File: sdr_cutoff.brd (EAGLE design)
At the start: 54.6 x 41.6 mm, 16 parts, among them IC1 7805T, K1 HY1Z-5V

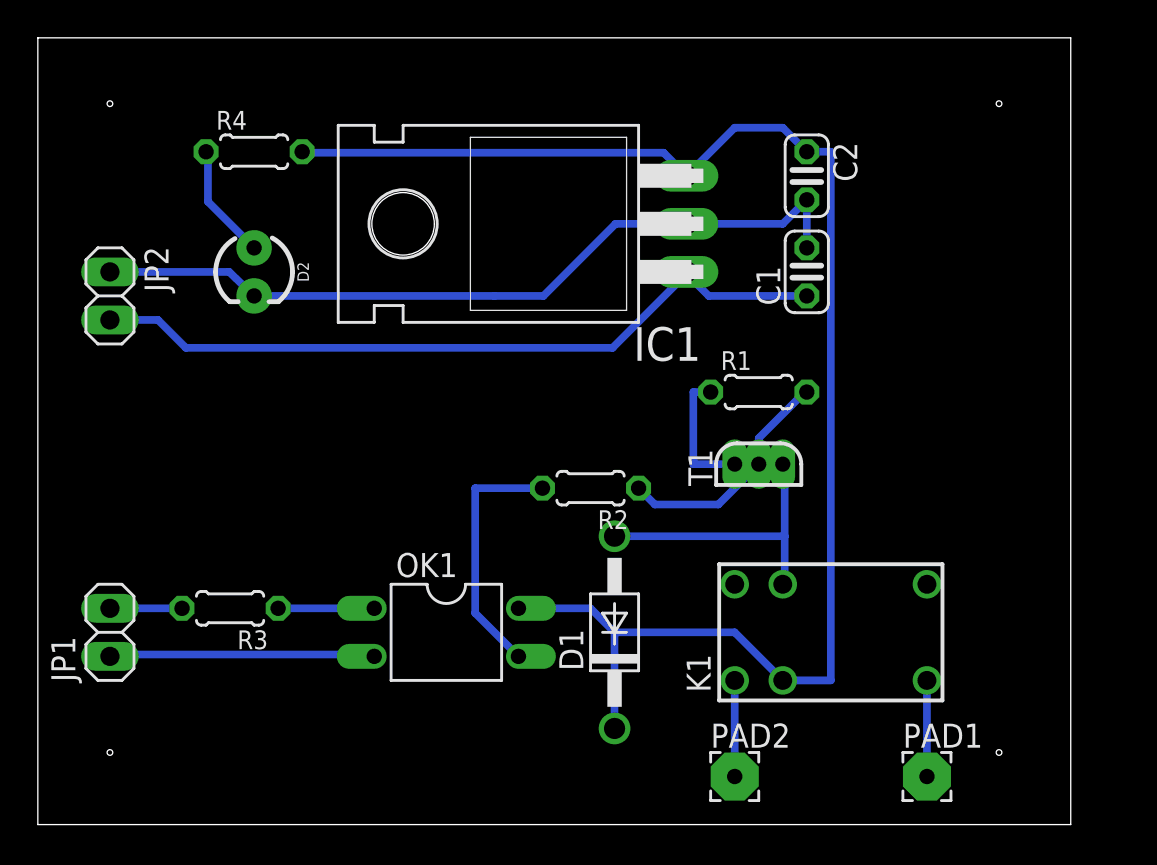
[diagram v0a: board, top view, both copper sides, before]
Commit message: Add files via upload
Corrected missing ground on DC block
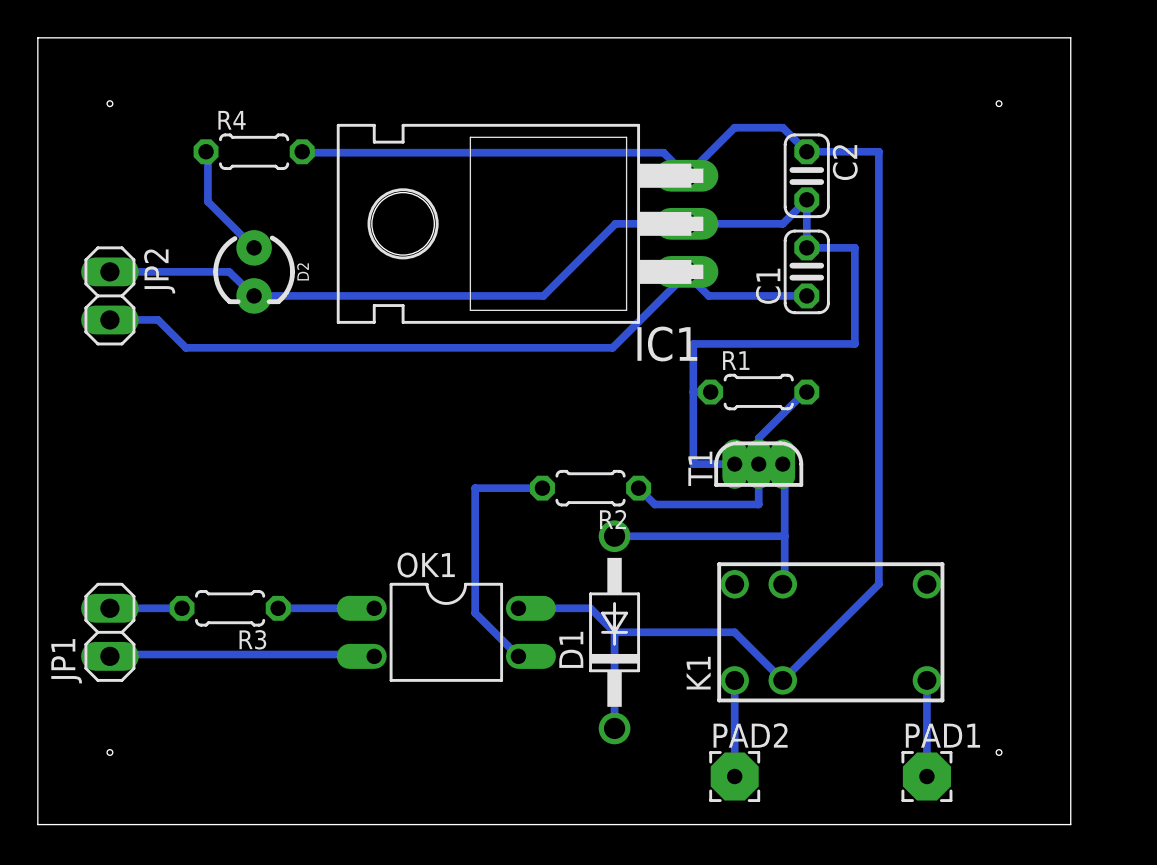
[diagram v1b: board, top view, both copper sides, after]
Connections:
- removed net N$7: C1.2, C2.2, D2.K, IC1.2, JP2.1
- net GND: now also C1.2, C2.2, D2.K, IC1.2, JP2.1
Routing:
- net GND: track 6.91 -> 67.7 mm
- net N$7: track 42.1 -> 0.00 mm
- net VCC: track 81.2 -> 83.3 mm
- net N$3: track 12.5 -> 13.8 mm
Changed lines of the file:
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@@
 <param name="rlMaxMicroViaInner" value="20mil"/>
 <param name="psTop" value="-1"/>
-<param name="psBottom" value="1"/>
+<param name="psBottom" value="2"/>
 <param name="psFirst" value="-1"/>
 <param name="psElongationLong" value="100"/>
@@
 <wire x1="40.5384" y1="22.86" x2="38.1" y2="20.4216" width="0.4064" layer="16"/>
 <wire x1="40.5384" y1="22.86" x2="40.64" y2="22.86" width="0.4064" layer="16"/>
-<wire x1="38.1" y1="19.05" x2="35.9664" y2="16.9164" width="0.4064" layer="16"/>
-<wire x1="35.9664" y1="16.9164" x2="32.6136" y2="16.9164" width="0.4064" layer="16"/>
+<wire x1="38.1" y1="19.05" x2="38.1" y2="16.9164" width="0.4064" layer="16"/>
+<wire x1="38.1" y1="16.9164" x2="32.6136" y2="16.9164" width="0.4064" layer="16"/>
 <wire x1="31.75" y1="17.78" x2="32.6136" y2="16.9164" width="0.4064" layer="16"/>
 <contactref element="T1" pad="2"/>
@@
 <contactref element="R1" pad="1"/>
 <wire x1="34.6456" y1="19.05" x2="36.83" y2="19.05" width="0.4064" layer="16"/>
+<wire x1="34.6456" y1="25.4" x2="34.6456" y2="22.86" width="0.4064" layer="16"/>
 <wire x1="34.6456" y1="22.86" x2="34.6456" y2="19.05" width="0.4064" layer="16"/>
 <wire x1="34.6456" y1="22.86" x2="35.56" y2="22.86" width="0.4064" layer="16"/>
 <contactref element="T1" pad="3"/>
+<contactref element="IC1" pad="2"/>
+<contactref element="JP2" pad="1"/>
+<contactref element="D2" pad="K"/>
+<contactref element="C2" pad="2"/>
+<contactref element="C1" pad="2"/>
+<wire x1="10.111153125" y1="29.21" x2="3.81" y2="29.21" width="0.4064" layer="16"/>
+<wire x1="10.111153125" y1="29.21" x2="11.43" y2="27.94" width="0.4064" layer="16"/>
+<wire x1="34.29" y1="31.8516" x2="34.29" y2="31.75" width="0.4064" layer="16"/>
+<wire x1="26.7208" y1="27.94" x2="11.43" y2="27.94" width="0.4064" layer="16"/>
+<wire x1="34.29" y1="31.75" x2="30.5308" y2="31.75" width="0.4064" layer="16"/>
+<wire x1="30.5308" y1="31.75" x2="26.7208" y2="27.94" width="0.4064" layer="16"/>
+<wire x1="40.64" y1="33.02" x2="40.64" y2="30.48" width="0.4064" layer="16"/>
+<wire x1="40.64" y1="33.02" x2="39.37" y2="31.75" width="0.4064" layer="16"/>
+<wire x1="39.37" y1="31.75" x2="34.29" y2="31.75" width="0.4064" layer="16"/>
+<wire x1="34.6456" y1="25.4" x2="43.18" y2="25.4" width="0.4064" layer="16"/>
+<wire x1="43.18" y1="25.4" x2="43.18" y2="30.48" width="0.4064" layer="16"/>
+<wire x1="43.18" y1="30.48" x2="40.64" y2="30.48" width="0.4064" layer="16"/>
 </signal>
 <signal name="VCC">
@@
 <wire x1="34.29" y1="34.29" x2="33.0708" y2="35.5092" width="0.4064" layer="16"/>
 <wire x1="14.0208" y1="35.5092" x2="13.97" y2="35.56" width="0.4064" layer="16"/>
-<wire x1="39.37" y1="7.62" x2="41.91" y2="7.62" width="0.4064" layer="16"/>
-<wire x1="41.91" y1="35.56" x2="41.91" y2="7.62" width="0.4064" layer="16"/>
+<wire x1="39.37" y1="7.62" x2="44.45" y2="12.7" width="0.4064" layer="16"/>
+<wire x1="44.45" y1="35.56" x2="44.45" y2="12.7" width="0.4064" layer="16"/>
 <wire x1="36.83" y1="36.83" x2="39.37" y2="36.83" width="0.4064" layer="16"/>
 <wire x1="39.37" y1="36.83" x2="40.64" y2="35.56" width="0.4064" layer="16"/>
 <wire x1="34.29" y1="34.29" x2="36.83" y2="36.83" width="0.4064" layer="16"/>
-<wire x1="40.64" y1="35.56" x2="41.91" y2="35.56" width="0.4064" layer="16"/>
+<wire x1="40.64" y1="35.56" x2="44.45" y2="35.56" width="0.4064" layer="16"/>
 </signal>
 <signal name="N$2">
@@
 <wire x1="3.81" y1="11.43" x2="7.62" y2="11.43" width="0.4064" layer="16"/>
 </signal>
-<signal name="N$7">
-<contactref element="IC1" pad="2"/>
-<contactref element="JP2" pad="1"/>
-<contactref element="D2" pad="K"/>
-<contactref element="C2" pad="2"/>
-<contactref element="C1" pad="2"/>
-<wire x1="10.111153125" y1="29.21" x2="3.81" y2="29.21" width="0.4064" layer="16"/>
-<wire x1="10.111153125" y1="29.21" x2="11.43" y2="27.94" width="0.4064" layer="16"/>
-<wire x1="34.29" y1="31.8516" x2="34.29" y2="31.75" width="0.4064" layer="16"/>
-<wire x1="26.7208" y1="27.94" x2="24.13" y2="27.94" width="0.4064" layer="16"/>
-<wire x1="24.13" y1="27.94" x2="11.43" y2="27.94" width="0.4064" layer="16"/>
-<wire x1="34.29" y1="31.75" x2="30.5308" y2="31.75" width="0.4064" layer="16"/>
-<wire x1="30.5308" y1="31.75" x2="26.7208" y2="27.94" width="0.4064" layer="16"/>
-<wire x1="40.64" y1="33.02" x2="40.64" y2="30.48" width="0.4064" layer="16"/>
-<wire x1="40.64" y1="33.02" x2="39.37" y2="31.75" width="0.4064" layer="16"/>
-<wire x1="39.37" y1="31.75" x2="34.29" y2="31.75" width="0.4064" layer="16"/>
-</signal>
 <signal name="N$8">

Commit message: Add files via upload
Corrected minor errors and finalised PCB layout
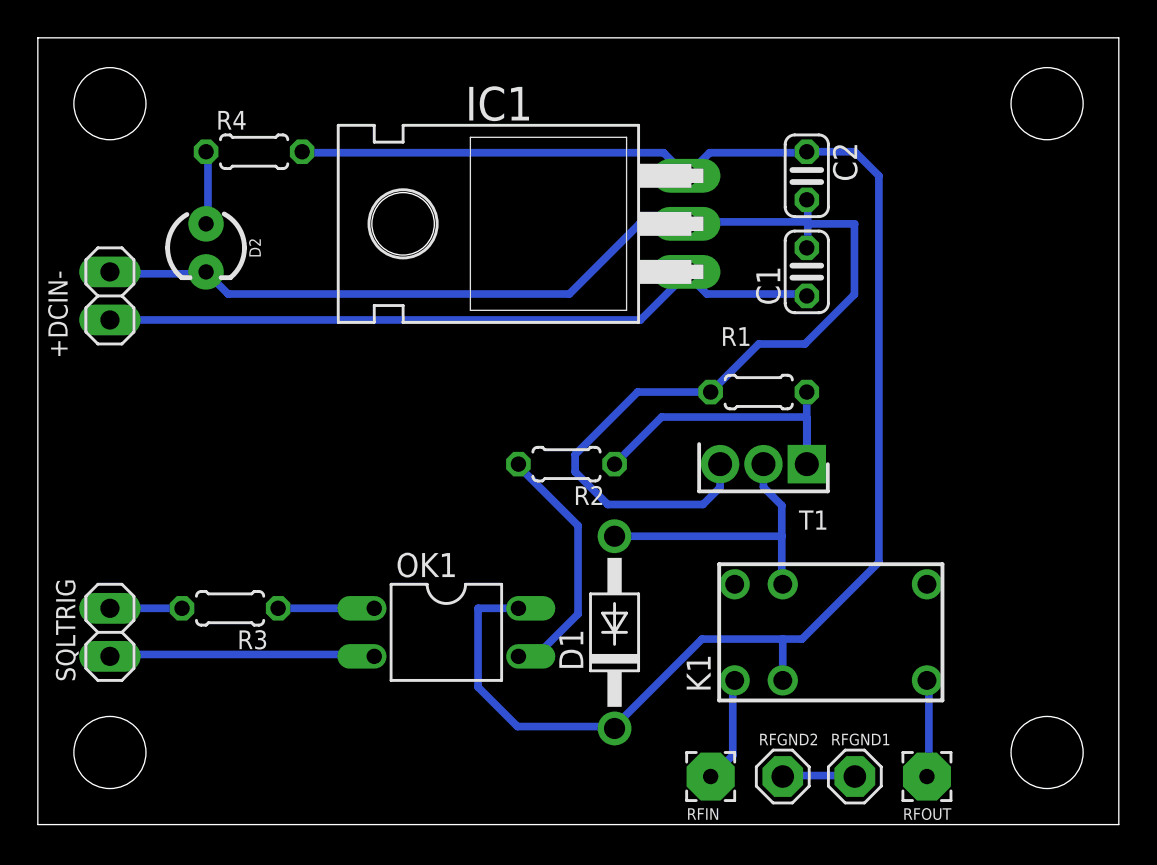
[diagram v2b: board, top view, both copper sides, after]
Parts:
- removed PAD2: (no value), wirepad:2,54/0,8
- added RFGND1, RFGND2: MCS08, solpad:MCS08
- added RFIN: (no value), wirepad:2,54/0,8
- T1: value (none) -> RFD14N05L; device zetex:E3LINE -> RFD14N05L:TO229P250X658X985-3P
- moved D2 2.84 mm to (8.89, 30.5)
- moved T1 2.54 mm to (40.6, 19.1), turned to 180 degrees
- moved R2 1.80 mm to (27.9, 19.1)
- renumbered JP1 to SQLTRIG, JP2 to +DCIN-, PAD1 to RFOUT
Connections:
- new net N$7: RFGND1.MP, RFGND2.MP
- net N$1: now also T1.2; no longer T1.1
- net N$3: now also T1.1; no longer T1.2
- net N$9: now also RFIN.1; no longer PAD2.1
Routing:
- net GND: track 67.7 -> 77.2 mm
- net N$7: track 0.00 -> 3.84 mm
- net N$3: track 13.8 -> 17.5 mm
- net VCC: track 83.3 -> 86.7 mm
- net N$10: track 6.15 -> 3.91 mm
- net N$8: track 39.6 -> 38.4 mm
- net N$9: track 5.08 -> 5.69 mm
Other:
- board size 54.6 x 41.6 mm -> 57.1 x 41.6 mm
